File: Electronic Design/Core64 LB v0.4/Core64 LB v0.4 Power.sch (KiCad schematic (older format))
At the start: 29 parts, among them IC1 NCP176AMX330TCG, IC2 TPS7A0533PDBVR, IC3 LP3961EMP-5.0, J18 5V0 Cur. Mon., J19 3V3 Cur. Mon., J3 Conn_01x08_Female, J8 S03B-PASK-2_LF__SN_, Q22 BSS315PH6327XTSA1, SW1 JS102011SAQN, U6 Micro_LiPo_Charger

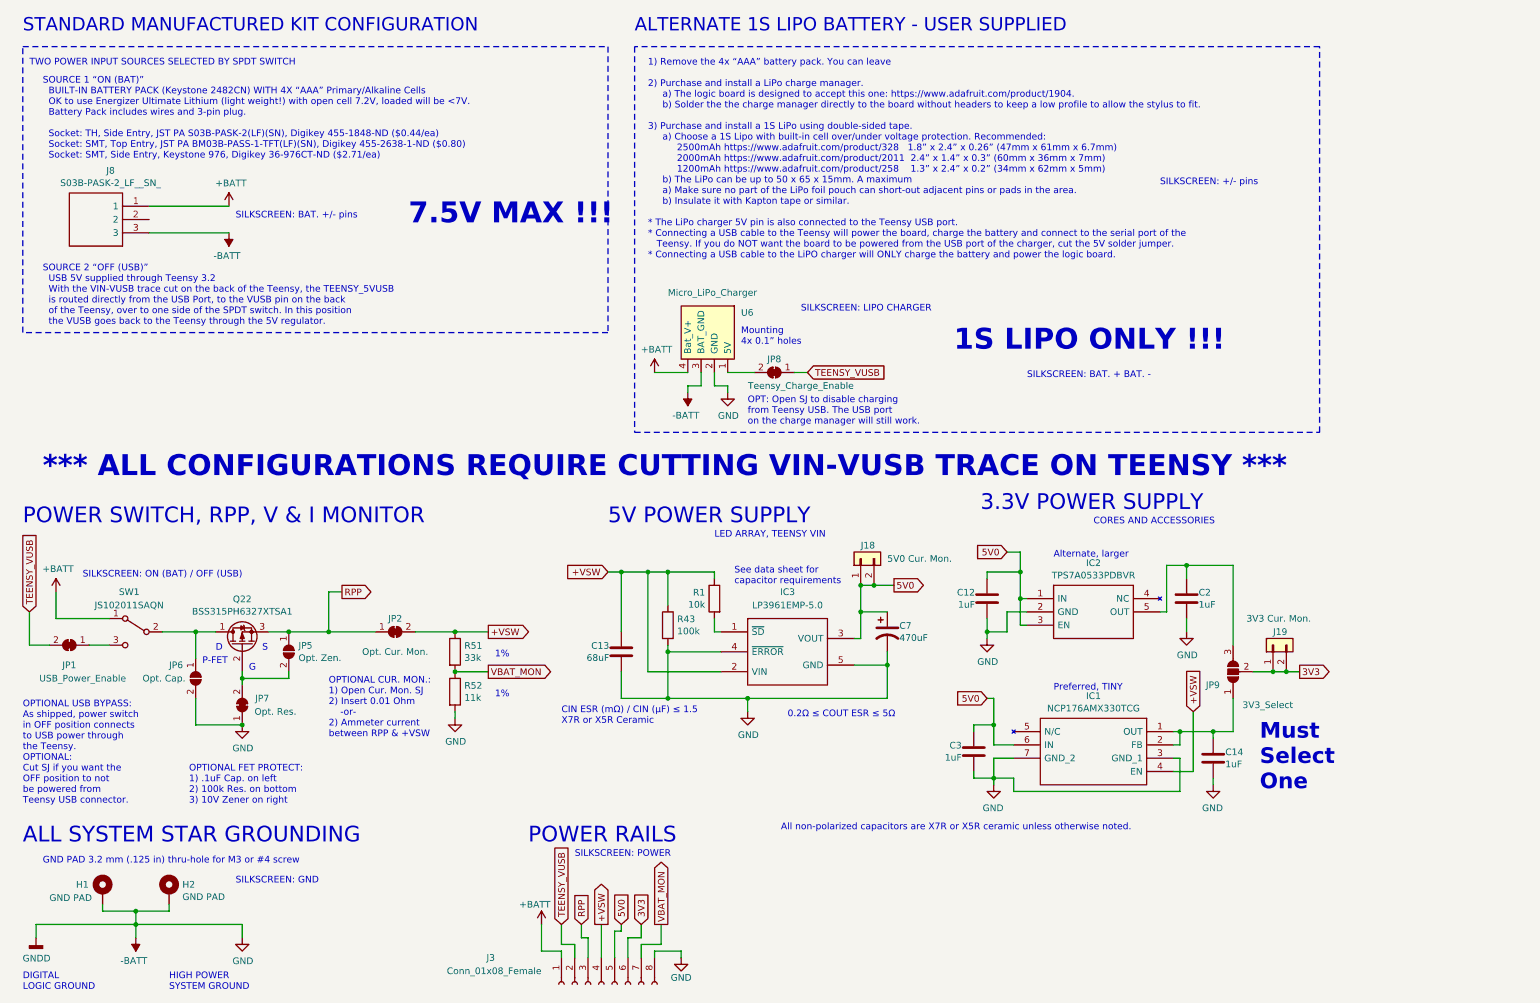
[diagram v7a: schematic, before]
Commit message: Review and tweak Logic Board (LB) schematic, pin usage
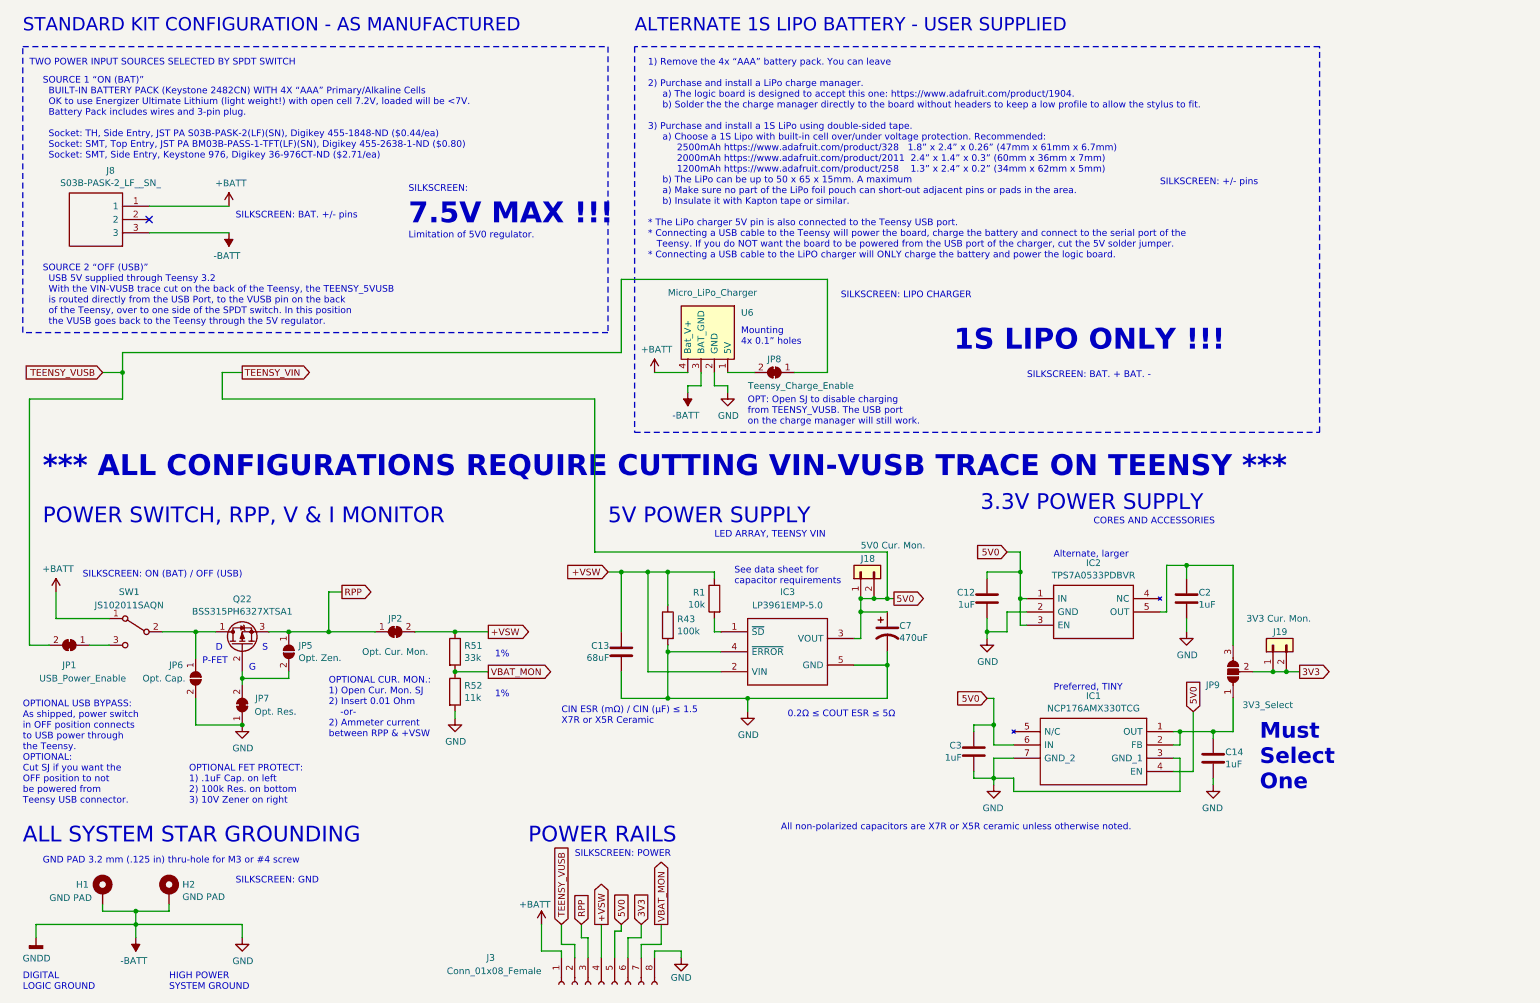
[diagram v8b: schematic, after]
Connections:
- net +VSW: no longer IC1.4 (EN)
- net 5V0: now also IC1.4 (EN)
- no-connect marks 0 -> 1
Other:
- note added: "Limitation of 5V0 regulator."
- note added: "OPT: Open SJ to disable charging\nfrom TEENSY_VUSB. The USB port\non the charge manager will still work."
- note added: "SILKSCREEN:"
- note added: "STANDARD KIT CONFIGURATION - AS MANUFACTURED"
- note removed: "OPT: Open SJ to disable charging\nfrom Teensy USB. The USB port\non the charge manager will still work."
- note removed: "STANDARD MANUFACTURED KIT CONFIGURATION"
- moved on the sheet: J18
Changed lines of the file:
@@
 	600  3000 600  850
 Text Notes 600  750  0    100  ~ 0
-STANDARD MANUFACTURED KIT CONFIGURATION
+STANDARD KIT CONFIGURATION - AS MANUFACTURED
 Text Notes 5200 750  0    100  ~ 0
 ALTERNATE 1S LIPO BATTERY - USER SUPPLIED
@@
 Text GLabel 10200 5550 2    50   Output ~ 0
 3V3
-Text Notes 600  4450 0    118  ~ 0
+Text Notes 750  4450 0    118  ~ 0
 POWER SWITCH, RPP, V & I MONITOR
 Text Notes 7800 4350 0    118  ~ 0
@@
 $EndComp
 Wire Wire Line
-	650  5100 650  5350
-Wire Wire Line
 	650  5350 800  5350
 Wire Wire Line
@@
 Wire Wire Line
 	2900 4950 3000 4950
-Text GLabel 7150 4900 2    50   Output ~ 0
+Text GLabel 7150 5000 2    50   Output ~ 0
 5V0
 Text GLabel 5100 7450 1    50   Input ~ 0
@@
 Text GLabel 4650 7450 1    50   Input ~ 0
 TEENSY_VUSB
-Text GLabel 650  5100 1    50   Input ~ 0
+Text GLabel 1200 3300 0    50   Input ~ 0
 TEENSY_VUSB
 Wire Wire Line
@@
 	1    0    0    -1
 $EndComp
-Text GLabel 6500 3300 2    50   Input ~ 0
-TEENSY_VUSB
 $Comp
 L power:-BATT #PWR0153
@@
 $EndComp
 Text Notes 6050 3700 0    50   ~ 0
-OPT: Open SJ to disable charging\nfrom Teensy USB. The USB port\non the charge manager will still work.
+OPT: Open SJ to disable charging\nfrom TEENSY_VUSB. The USB port\non the charge manager will still work.
 Wire Wire Line
 	5900 3300 6100 3300
-Wire Wire Line
-	6400 3300 6500 3300
 Text Notes 6300 6750 0    50   ~ 0
 All non-polarized capacitors are X7R or X5R ceramic unless otherwise noted.
@@
 	9300 6000 9550 6000
 Text GLabel 9400 5850 1    50   Input ~ 0
-+VSW
+5V0
 Wire Wire Line
 	9550 6000 9550 6050
@@
 	6850 5300 6900 5300
 Wire Wire Line
-	6900 4900 6900 5100
+	6900 5000 6900 5100
 Wire Wire Line
 	5450 4800 5450 5050
@@
 Text Notes 2200 7150 0    50   ~ 0
 SILKSCREEN: GND
-Text Notes 6450 2850 0    50   ~ 0
+Text Notes 6750 2750 0    50   ~ 0
 SILKSCREEN: LIPO CHARGER
 Text Notes 8150 3350 0    50   ~ 0
@@
 L Connector_Generic:Conn_01x02 J18
 U 1 1 5F8E6AE3
-P 6900 4700
-F 0 "J18" V 7000 4700 50  0000 R CNN
-F 1 "5V0 Cur. Mon." V 6900 4500 50  0000 R CNN
-F 2 "Connector_PinSocket_2.54mm:PinSocket_1x02_P2.54mm_Vertical" H 6900 4700 50  0001 C CNN
-F 3 "~" H 6900 4700 50  0001 C CNN
-	1    6900 4700
+P 6900 4800
+F 0 "J18" V 7000 4800 50  0000 R CNN
+F 1 "5V0 Cur. Mon." V 7100 4800 50  0000 R CNN
+F 2 "Connector_PinSocket_2.54mm:PinSocket_1x02_P2.54mm_Vertical" H 6900 4800 50  0001 C CNN
+F 3 "~" H 6900 4800 50  0001 C CNN
+	1    6900 4800
 	0    -1   -1   0
 $EndComp
 Wire Wire Line
-	7000 4900 7150 4900
-Wire Wire Line
-	6900 4900 7000 4900
-Connection ~ 6900 4900
-Connection ~ 7000 4900
+	7000 5000 7100 5000
+Wire Wire Line
+	6900 5000 7000 5000
+Connection ~ 6900 5000
+Connection ~ 7000 5000
 Wire Wire Line
 	6900 5100 6900 5300
@@
 Wire Wire Line
 	8050 6350 7900 6350
+Connection ~ 7100 5000
+Wire Wire Line
+	7100 5000 7150 5000
+Text GLabel 2250 3300 2    50   Output ~ 0
+TEENSY_VIN
+NoConn ~ 1550 2150
+Wire Wire Line
+	1200 3300 1350 3300
+Wire Wire Line
+	1350 3300 1350 3500
+Wire Wire Line
+	1350 3500 650  3500
+Wire Wire Line
+	650  3500 650  5350
+Wire Wire Line
+	2250 3300 2100 3300
+Wire Wire Line
+	2100 3300 2100 3500
+Wire Wire Line
+	2100 3500 4900 3500
+Wire Wire Line
+	4900 3500 4900 4650
+Wire Wire Line
+	4900 4650 7100 4650
+Wire Wire Line
+	7100 4650 7100 5000
+Wire Wire Line
+	1350 3300 1350 3150
+Wire Wire Line
+	1350 3150 5100 3150
+Wire Wire Line
+	5100 3150 5100 2600
+Wire Wire Line
+	5100 2600 6650 2600
+Wire Wire Line
+	6650 2600 6650 3300
+Wire Wire Line
+	6400 3300 6650 3300
+Connection ~ 1350 3300
+Text Notes 3500 1950 0    50   ~ 0
+SILKSCREEN:
+Text Notes 3500 2300 0    50   ~ 0
+Limitation of 5V0 regulator.
 $EndSCHEMATC
